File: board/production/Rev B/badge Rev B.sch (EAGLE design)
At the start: 68 parts, among them IC1 TLV62569, J1 5051101092, J2 M05X2X1.27, U1 BMD-300

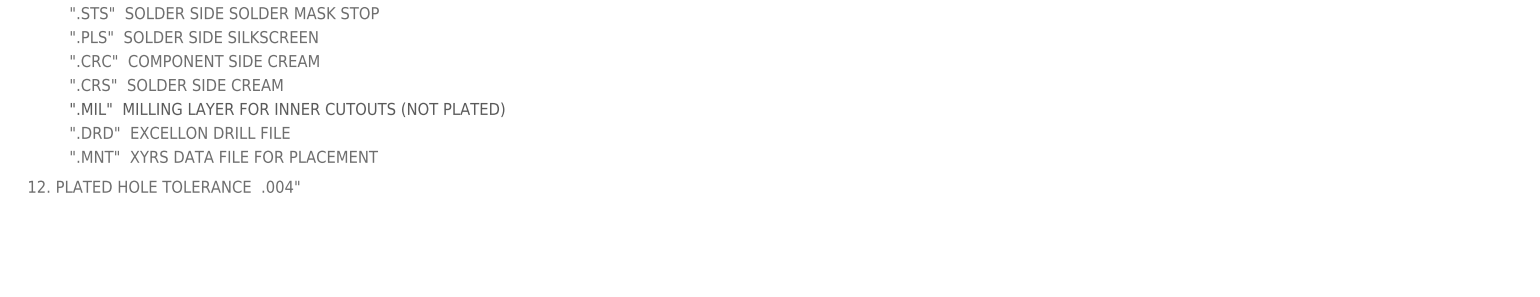
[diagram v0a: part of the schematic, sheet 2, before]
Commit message: make note about hole in center of PCB
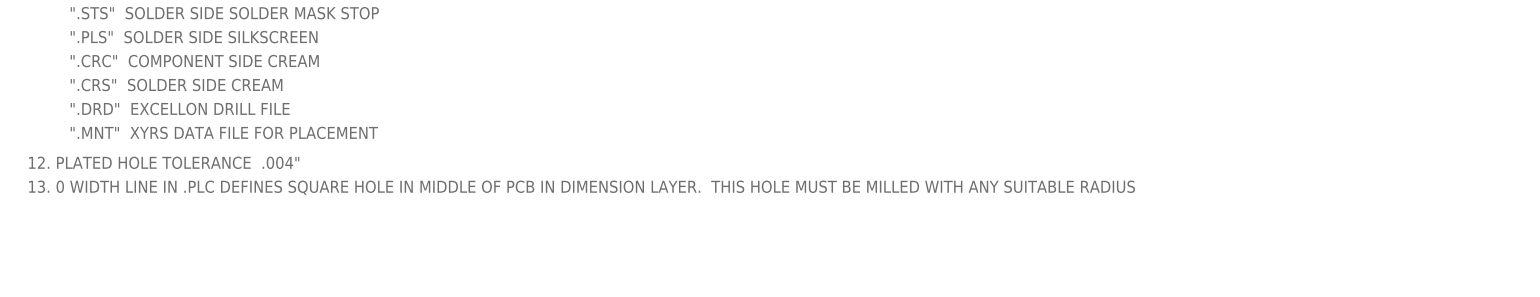
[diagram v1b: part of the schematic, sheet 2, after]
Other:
- note added: "13. 0 WIDTH LINE IN .PLC DEFINES SQUARE HOLE IN MIDDLE OF PCB IN DIMENSION LAYER. THIS HOLE MUST BE MILLED WITH ANY SUITABLE RADIUS"
- note removed: "".MIL" MILLING LAYER FOR INNER CUTOUTS (NOT PLATED)"
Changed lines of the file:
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@@
 <setting verticaltext="up"/>
 </settings>
-<grid distance="0.05" unitdist="inch" unit="inch" style="lines" multiple="1" display="no" altdistance="0.01" altunitdist="inch" altunit="inch"/>
+<grid distance="0.1" unitdist="inch" unit="inch" style="lines" multiple="1" display="no" altdistance="0.01" altunitdist="inch" altunit="inch"/>
 <layers>
 <layer number="1" name="Top" color="4" fill="1" visible="no" active="no"/>
@@
 <text x="25.4" y="185.42" size="2.54" layer="95">".STC"  COMPONENT SIDE SOLDER MASK STOP</text>
 <text x="25.4" y="165.1" size="2.54" layer="95">".STS"  SOLDER SIDE SOLDER MASK STOP</text>
-<text x="25.4" y="139.7" size="2.54" layer="95">".DRD"  EXCELLON DRILL FILE</text>
-<text x="25.4" y="134.62" size="2.54" layer="95">".MNT"  XYRS DATA FILE FOR PLACEMENT</text>
+<text x="25.4" y="144.78" size="2.54" layer="95">".DRD"  EXCELLON DRILL FILE</text>
+<text x="25.4" y="139.7" size="2.54" layer="95">".MNT"  XYRS DATA FILE FOR PLACEMENT</text>
 <text x="229.87" y="52.07" size="2.54" layer="95">LAYER 1 - COMPONENT SIDE, 1oz FINISH</text>
 <text x="229.87" y="6.35" size="2.54" layer="95">LAYER 2 - SOLDER SIDE, 1oz FINISH</text>
@@
 <text x="181.61" y="29.21" size="2.1844" layer="95">60 mil</text>
 <text x="161.417" y="63.119" size="3.175" layer="95">LAYER STACKUP DETAIL</text>
-<text x="16.51" y="128.27" size="2.54" layer="95">12. PLATED HOLE TOLERANCE  .004"</text>
-<text x="25.4" y="144.78" size="2.54" layer="97">".MIL"  MILLING LAYER FOR INNER CUTOUTS (NOT PLATED)</text>
+<text x="16.51" y="133.35" size="2.54" layer="95">12. PLATED HOLE TOLERANCE  .004"</text>
 <text x="17.78" y="203.2" size="2.54" layer="95">10. 15mil MAX RADIUS  INSIDE MILLING CORNERS FOR SMALL RECTANGULAR OPENINGS</text>
 <text x="25.4" y="175.26" size="2.54" layer="95">".DIM"  DIMENSION LAYER WITH OUTSIDE DIMENSIONS IN MM</text>
+<text x="16.51" y="128.27" size="2.54" layer="95">13. 0 WIDTH LINE IN .PLC DEFINES SQUARE HOLE IN MIDDLE OF PCB IN DIMENSION LAYER.  THIS HOLE MUST BE MILLED WITH ANY SUITABLE RADIUS</text>
 </plain>
 <instances>
